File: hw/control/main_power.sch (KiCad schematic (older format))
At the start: 15 parts, among them U201 LM2596T-ADJ

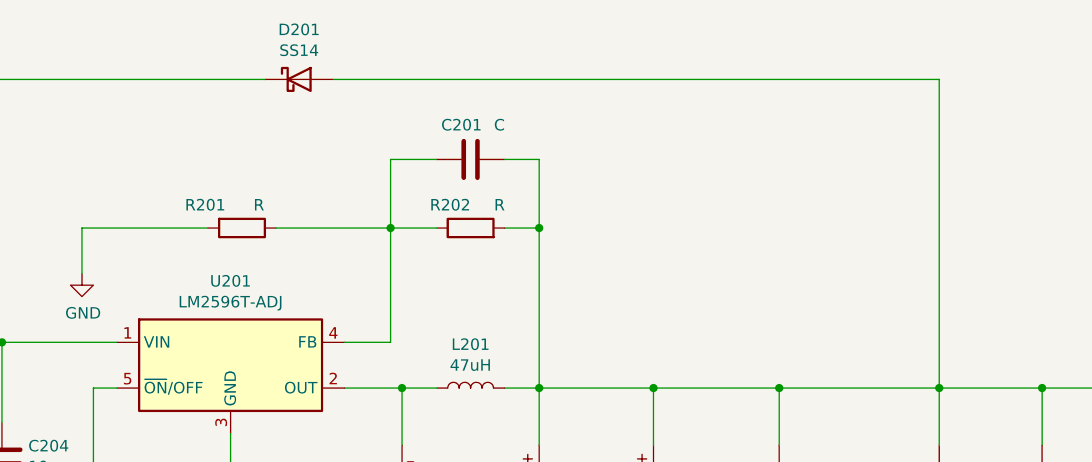
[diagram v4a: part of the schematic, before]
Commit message: [hw] Calculate main power supply feedback res.
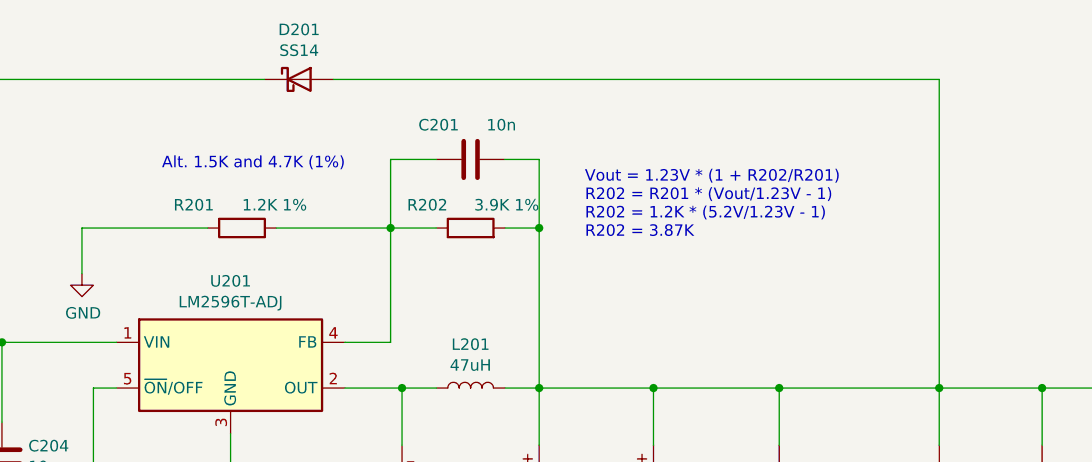
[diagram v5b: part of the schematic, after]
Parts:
- C201: value C -> 10n
- R201: value R -> 1.2K 1%
- R202: value R -> 3.9K 1%
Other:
- note added: "Alt. 1.5K and 4.7K (1%)"
- note added: "Vout = 1.23V * (1 + R202/R201)\nR202 = R201 * (Vout/1.23V - 1)\nR202 = 1.2K * (5.2V/1.23V - 1)\nR202 = 3.87K"
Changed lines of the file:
@@
-$EndComp
-$Comp
-L Device:R R201
-U 1 1 61481E1C
-P 5700 3000
-F 0 "R201" V 5600 2750 50  0000 L CNN
-F 1 "R" V 5600 3050 50  0000 L CNN
-F 2 "Resistor_SMD:R_0805_2012Metric_Pad1.20x1.40mm_HandSolder" V 5630 3000 50  0001 C CNN
-F 3 "~" H 5700 3000 50  0001 C CNN
-	1    5700 3000
-	0    1    1    0
-$EndComp
-$Comp
-L Device:R R202
-U 1 1 614831F3
-P 6700 3000
-F 0 "R202" V 6800 3000 50  0000 L CNN
-F 1 "R" V 6800 2850 50  0000 L CNN
-F 2 "Resistor_SMD:R_0805_2012Metric_Pad1.20x1.40mm_HandSolder" V 6630 3000 50  0001 C CNN
-F 3 "~" H 6700 3000 50  0001 C CNN
-	1    6700 3000
-	0    -1   -1   0
 $EndComp
 $Comp
@@
 U 1 1 61484750
 P 6700 2700
-F 0 "C201" V 6850 2650 50  0000 L CNN
-F 1 "C" V 6850 2550 50  0000 L CNN
+F 0 "C201" V 6850 2750 50  0000 L CNN
+F 1 "10n" V 6850 2500 50  0000 L CNN
 F 2 "Capacitor_SMD:C_0805_2012Metric_Pad1.18x1.45mm_HandSolder" H 6738 2550 50  0001 C CNN
 F 3 "~" H 6700 2700 50  0001 C CNN
@@
 Wire Wire Line
 	8050 4500 8750 4500
+Text Notes 7200 3050 0    50   ~ 0
+Vout = 1.23V * (1 + R202/R201)\nR202 = R201 * (Vout/1.23V - 1)\nR202 = 1.2K * (5.2V/1.23V - 1)\nR202 = 3.87K
+$Comp
+L Device:R R202
+U 1 1 614831F3
+P 6700 3000
+F 0 "R202" V 6800 3100 50  0000 L CNN
+F 1 "3.9K 1%" V 6800 2700 50  0000 L CNN
+F 2 "Resistor_SMD:R_0805_2012Metric_Pad1.20x1.40mm_HandSolder" V 6630 3000 50  0001 C CNN
+F 3 "~" H 6700 3000 50  0001 C CNN
+	1    6700 3000
+	0    -1   -1   0
+$EndComp
+$Comp
+L Device:R R201
+U 1 1 61481E1C
+P 5700 3000
+F 0 "R201" V 5600 2700 50  0000 L CNN
+F 1 "1.2K 1%" V 5600 3000 50  0000 L CNN
+F 2 "Resistor_SMD:R_0805_2012Metric_Pad1.20x1.40mm_HandSolder" V 5630 3000 50  0001 C CNN
+F 3 "~" H 5700 3000 50  0001 C CNN
+	1    5700 3000
+	0    1    1    0
+$EndComp
+Text Notes 5350 2750 0    50   ~ 0
+Alt. 1.5K and 4.7K (1%)
 $EndSCHEMATC
